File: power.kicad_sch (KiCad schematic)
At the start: 6 parts

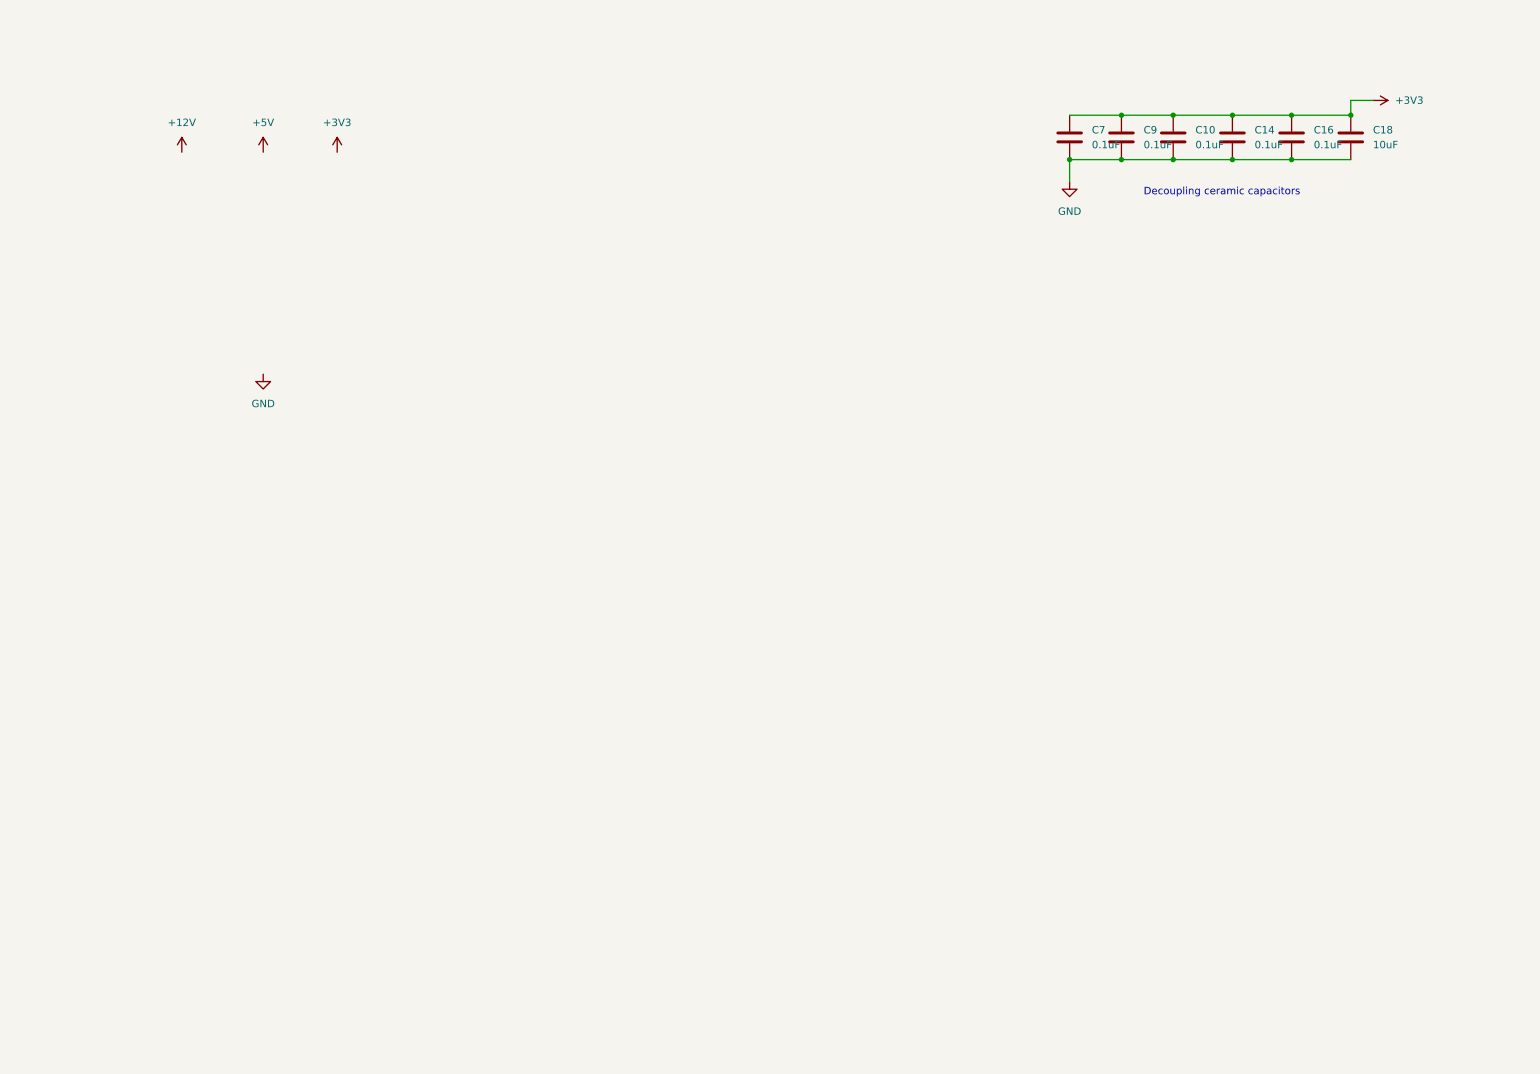
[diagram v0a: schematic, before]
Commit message: Add files via upload
changed 12v power to ICW6215, added 5 and 3v3
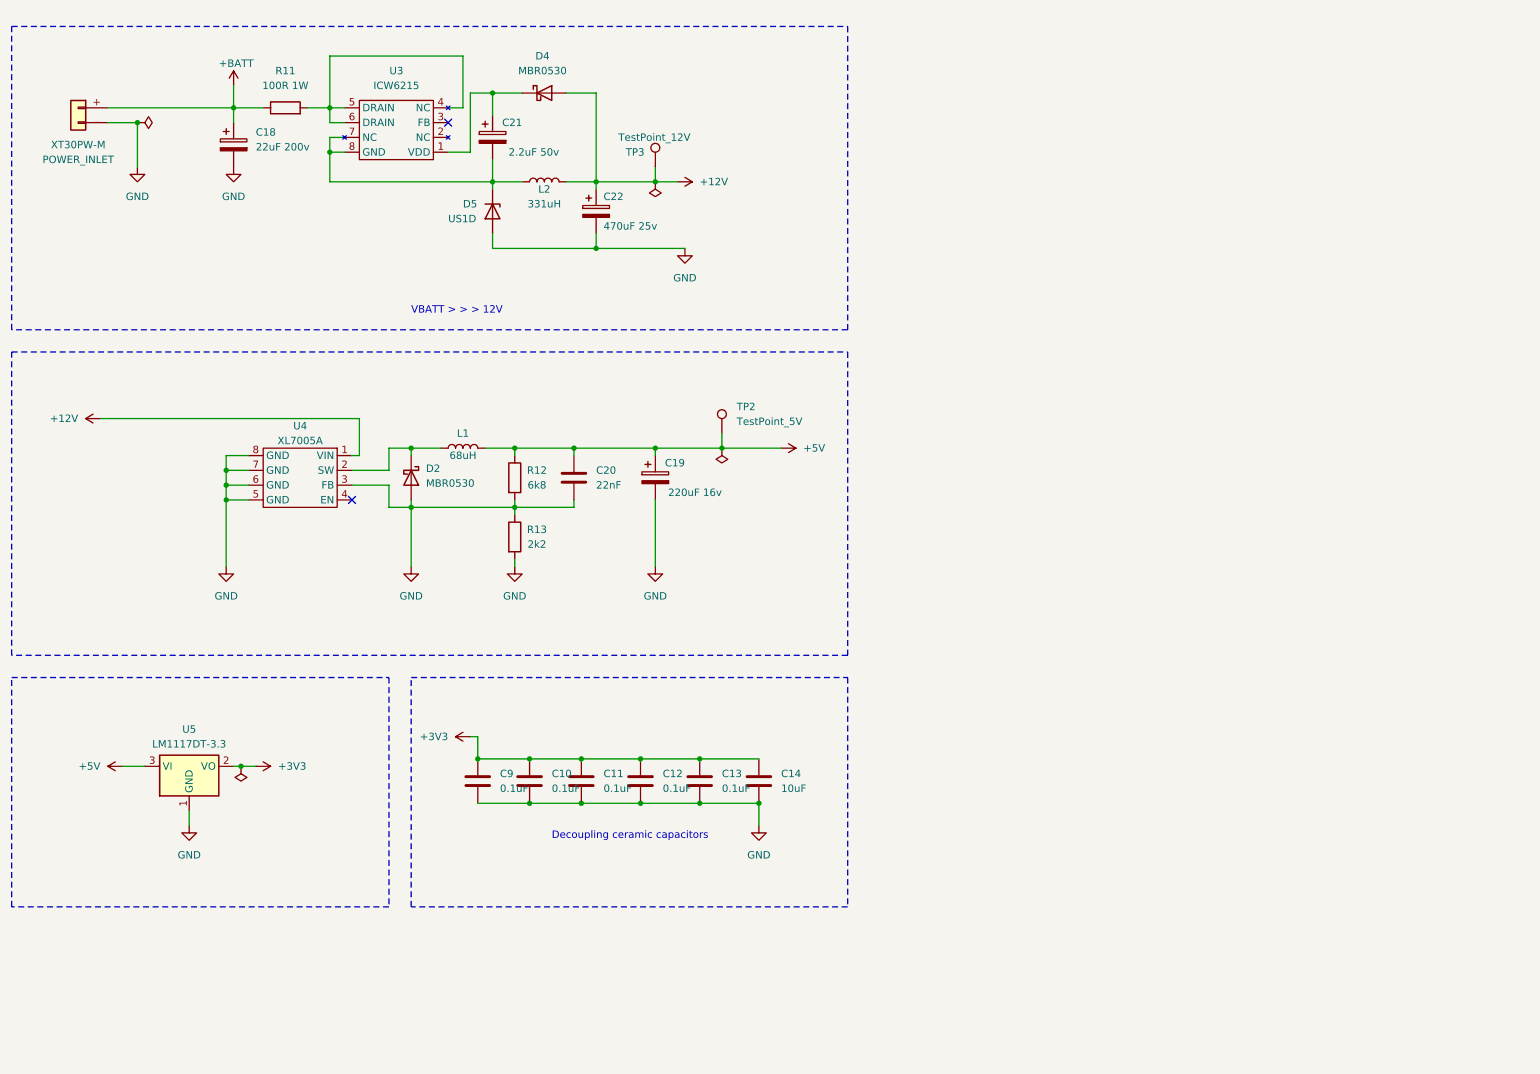
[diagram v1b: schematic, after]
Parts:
- added C18: 22uF 200v, symbol Device:C_Polarized
- added C19: 220uF 16v, symbol Device:C_Polarized
- added C20: 22nF, symbol Device:C
- added C21: 2.2uF 50v, symbol Device:C_Polarized
- added C22: 470uF 25v, symbol Device:C_Polarized
- added D2, D4: MBR0530, Diode_SMD:D_SOD-123, symbol Diode:MBR0530
- added D5: US1D, symbol Device:D_Zener
- added L1: 68uH, symbol Device:L
- added L2: 331uH, symbol Device:L
- added POWER_INLET: XT30PW-M, symbol Connector_Generic:Conn_01x02
- added R11: 100R 1W, symbol Device:R
- added R12: 6k8, symbol Device:R
- added R13: 2k2, symbol Device:R
- added TP2: TestPoint_5V, symbol Connector:TestPoint
- added TP3: TestPoint_12V, symbol Connector:TestPoint
- added U3: ICW6215, symbol 4shift:ICW6215
- added U4: XL7005A, symbol 4shift:XL7005a
- added U5: LM1117DT-3.3, Package_TO_SOT_SMD:TO-252-3_TabPin2, symbol Regulator_Linear:LM1117DT-3.3
- renumbered C9 to C10, C10 to C11, C14 to C12, C16 to C13, C18 to C14, C7 to C9
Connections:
- net +12V: now also C22.1, D4.2 (A), L2.2, TP3.1, U4.1 (VIN)
- net +3V3: now also U5.2 (VO)
- net +5V: now also C19.1, C20.1, L1.2, R12.1, TP2.1, U5.3 (VI)
- net GND: now also C18.2, C19.2, C20.2, C22.2, D2.2 (A), D5.2 (A), POWER_INLET._ (Pin_2), R12.2, R13.1, R13.2, U4.3 (FB), U4.5 (GND), U4.6 (GND), U4.7 (GND), U4.8 (GND), U5.1 (GND)
- new net: C21.1, D4.1 (K), U3.1 (VDD)
- new net: C21.2, D5.1 (K), L2.1, U3.7 (NC), U3.8 (GND)
- new net: R11.2, U3.4 (NC), U3.5 (DRAIN), U3.6 (DRAIN)
- new net: D2.1 (K), L1.1, U4.2 (SW)
- new net +BATT: C18.1, POWER_INLET.+ (Pin_1), R11.1
- no-connect marks 0 -> 2
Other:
- note added: "VBATT > > > 12V"
- moved on the sheet: C10, C11, C12, C13, C14, C9

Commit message: Add files via upload
Added hivoltage cirquit. TODO - add powon (VT19 on MSX)
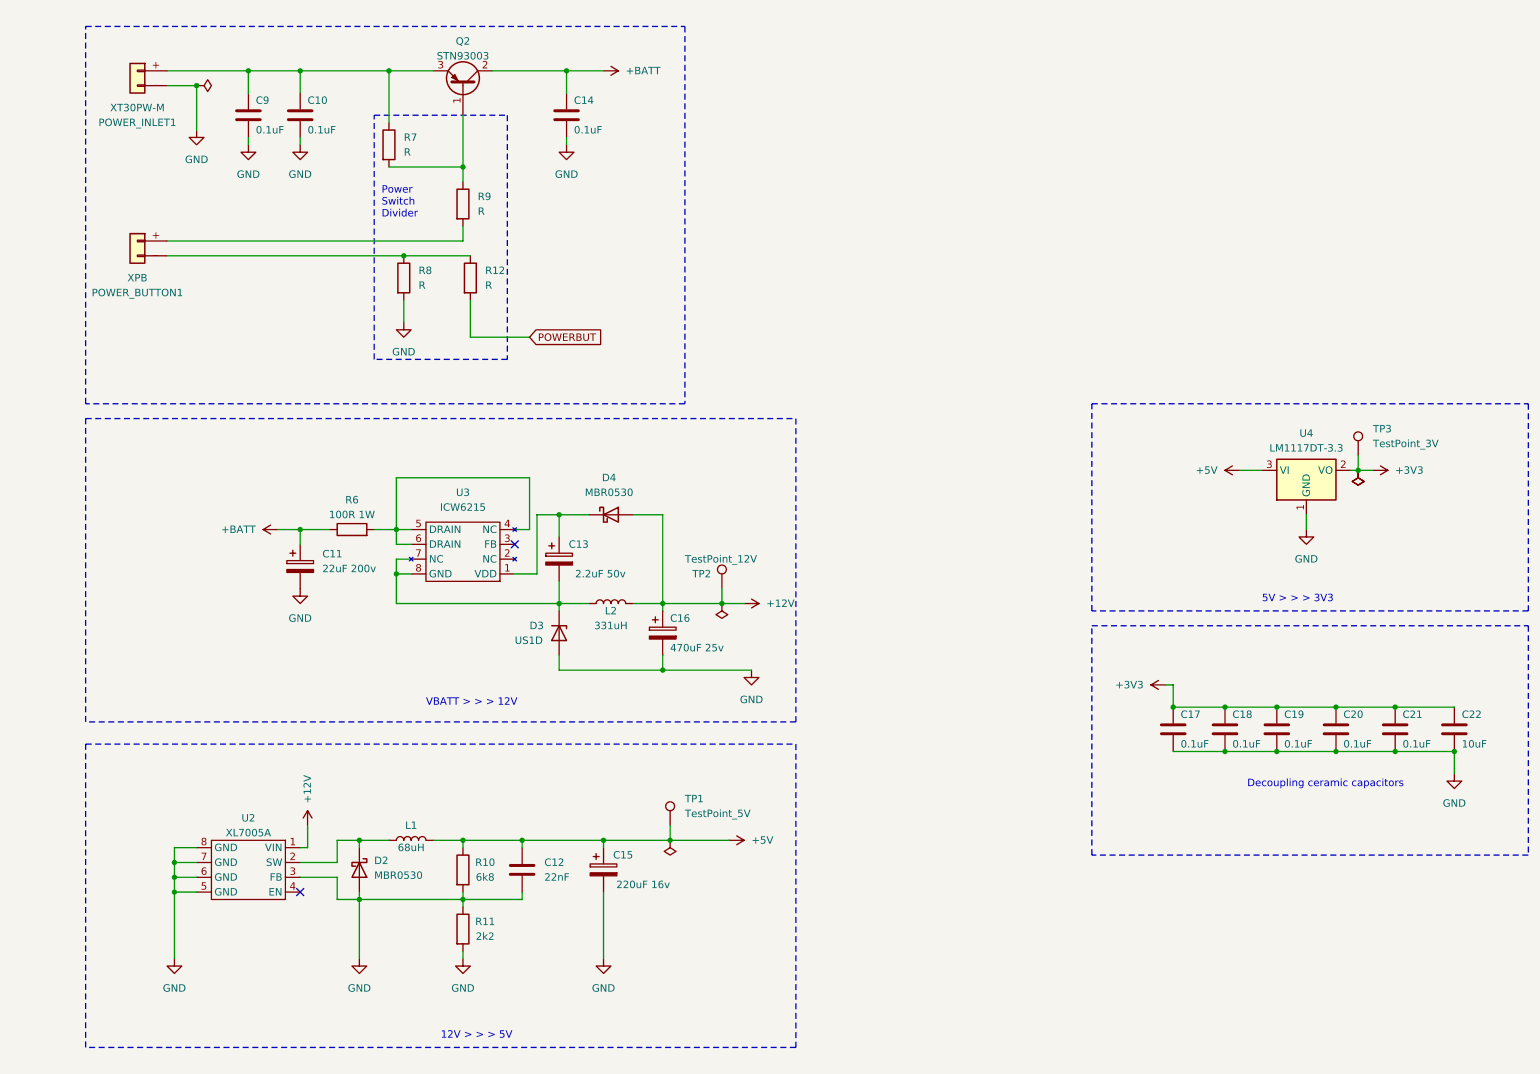
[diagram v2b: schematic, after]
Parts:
- removed POWER_INLET: XT30PW-M, symbol Connector_Generic:Conn_01x02
- removed U5: LM1117DT-3.3, Package_TO_SOT_SMD:TO-252-3_TabPin2, symbol Regulator_Linear:LM1117DT-3.3
- added C10, C14, C9: 0.1uF, Capacitor_SMD:C_0402_1005Metric, symbol Device:C
- added POWER_BUTTON1: XPB, symbol Connector_Generic:Conn_01x02
- added POWER_INLET1: XT30PW-M, symbol Connector_Generic:Conn_01x02
- added Q2: STN93003, Package_TO_SOT_SMD:SOT-223-3_TabPin2, symbol 4shift:STN93003
- added R12, R7, R8, R9: R, symbol Device:R
- added TP3: TestPoint_3V, symbol Connector:TestPoint
- added U4: LM1117DT-3.3, Package_TO_SOT_SMD:TO-252-3_TabPin2, symbol Regulator_Linear:LM1117DT-3.3
- renumbered C18 to C11, C20 to C12, C21 to C13, C19 to C15, C22 to C16, C9 to C17, C10 to C18, C11 to C19, C12 to C20, C13 to C21, C14 to C22, D5 to D3, R12 to R10, R13 to R11, R11 to R6, TP2 to TP1, TP3 to TP2, U4 to U2
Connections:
- net +3V3: now also TP3.1, U4.2 (VO)
- net +5V: now also U4.3 (VI)
- net +BATT: now also C14.1, Q2.2 (C)
- net GND: now also C10.2, C14.2, C9.2, POWER_INLET1._ (Pin_2), R8.2, U4.1 (GND)
- new net: C10.1, C9.1, POWER_INLET1.+ (Pin_1), Q2.3 (E), R7.1
- new net: Q2.1 (B), R7.2, R9.1
- new net: POWER_BUTTON1.+ (Pin_1), R9.2
- new net: POWER_BUTTON1._ (Pin_2), R12.1, R8.1
- new net POWERBUT: R12.2
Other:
- note added: "12V > > > 5V"
- note added: "5V > > > 3V3"
- note added: "Power Switch Divider"
- moved on the sheet: C11, C12, C13, C15, C16, C17, C18, C19, C20, C21, C22, D2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

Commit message: Add files via upload
Add +12 and +5 outlets, change buzzer transistor, minor updates
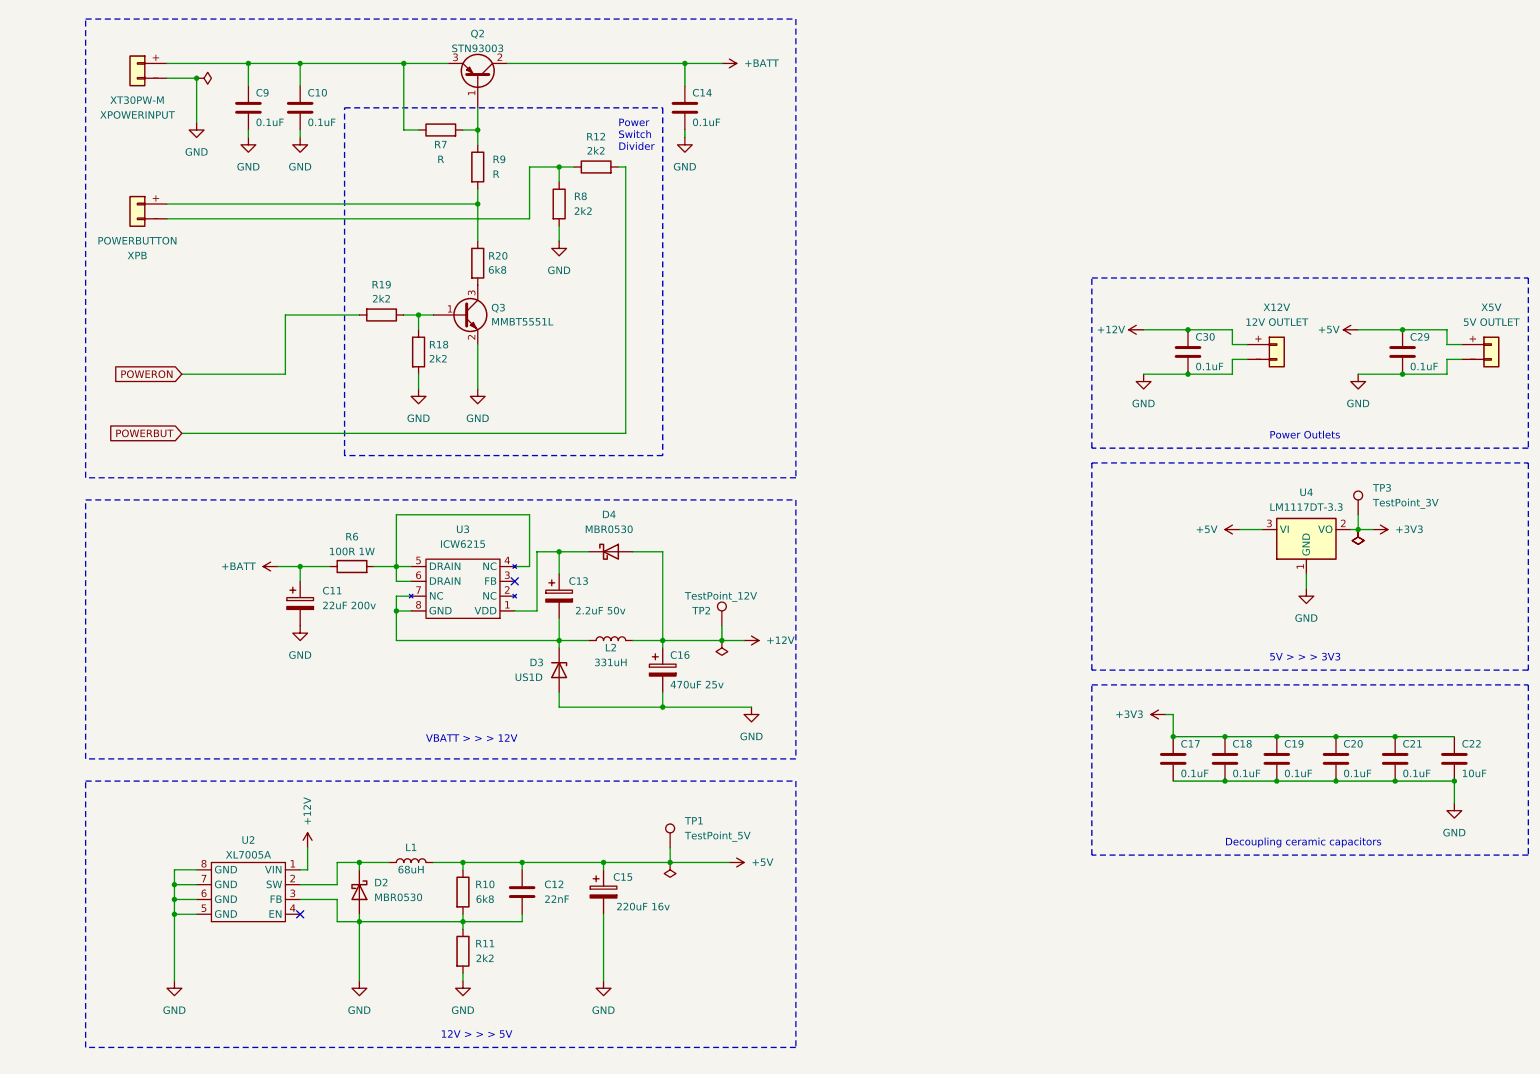
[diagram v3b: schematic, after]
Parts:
- added C29, C30: 0.1uF, Capacitor_SMD:C_0402_1005Metric, symbol Device:C
- added Q3: MMBT5551L, Package_TO_SOT_SMD:SOT-23, symbol Transistor_BJT:MMBT5551L
- added R18, R19: 2k2, symbol Device:R
- added R20: 6k8, symbol Device:R
- added X12V: 12V OUTLET, symbol Connector_Generic:Conn_01x02
- added X5V: 5V OUTLET, symbol Connector_Generic:Conn_01x02
- R12, R8: value R -> 2k2
- XPB: renamed from POWER_BUTTON1; value XPB -> POWERBUTTON
- renumbered POWER_INLET1 to XPOWERINPUT
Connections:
- net +12V: now also C30.1, X12V.+ (Pin_1)
- net +5V: now also C29.1, X5V.+ (Pin_1)
- net GND: now also C29.2, C30.2, Q3.2 (E), R18.2, X12V._ (Pin_2), X5V._ (Pin_2)
- net at R9.2, XPB.+ (Pin_1): now also R20.1
- new net: Q3.3 (C), R20.2
- new net: Q3.1 (B), R18.1, R19.1
- new net POWERON: R19.2
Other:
- note added: "Power Outlets"
- moved on the sheet: C10, C11, C12, C13, C14, C15, C16, C17, C18, C19, C20, C21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

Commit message: Divider, gate, mtr button, testpoints, minors
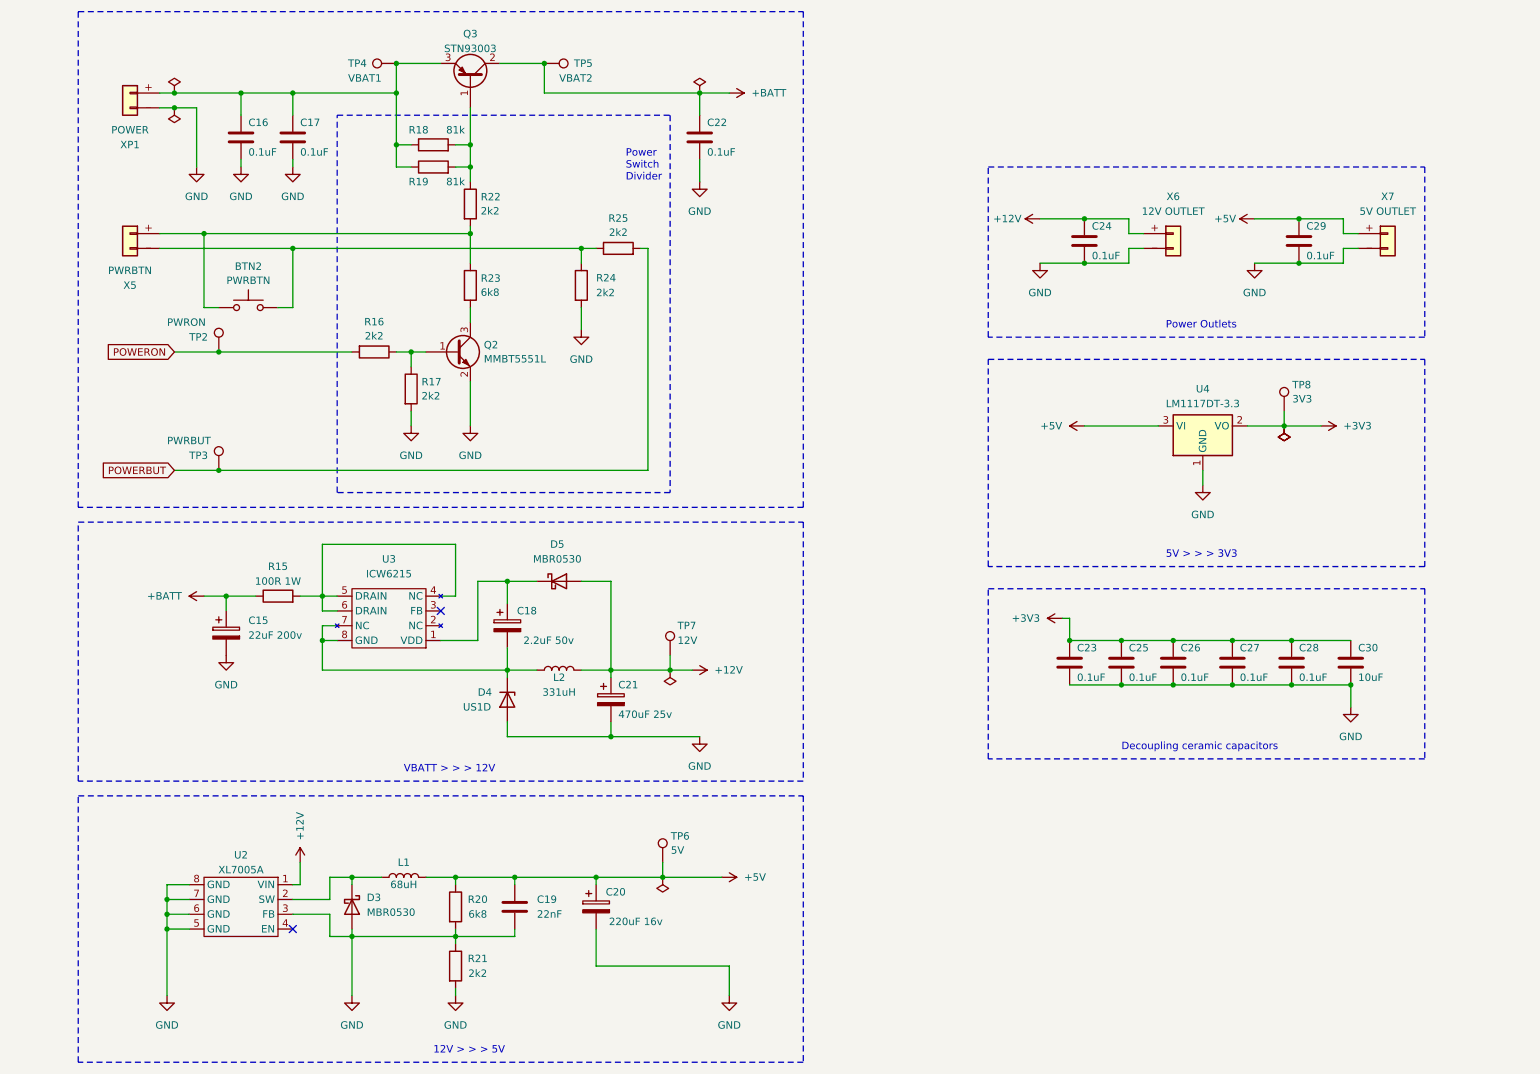
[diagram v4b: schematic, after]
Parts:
- added BTN2: PWRBTN, symbol Switch:SW_Push
- added R18: 81k, symbol Device:R
- added TP2: PWRON, symbol Connector:TestPoint
- added TP3: PWRBUT, symbol Connector:TestPoint
- added TP4: VBAT1, symbol Connector:TestPoint
- added TP5: VBAT2, symbol Connector:TestPoint
- R19: renamed from R7; value R -> 81k
- R22: renamed from R9; value R -> 2k2
- TP6: renamed from TP1; value TestPoint_5V -> 5V
- TP7: renamed from TP2; value TestPoint_12V -> 12V
- TP8: renamed from TP3; value TestPoint_3V -> 3V3
- X5: renamed from XPB; value POWERBUTTON -> PWRBTN
- XP1: renamed from XPOWERINPUT; value XT30PW-M -> POWER
- renumbered C11 to C15, C9 to C16, C10 to C17, C13 to C18, C12 to C19, C15 to C20, C16 to C21, C14 to C22, C17 to C23, C30 to C24, C18 to C25, C19 to C26, C20 to C27, C21 to C28, C22 to C30, D2 to D3, D3 to D4, D4 to D5, Q3 to Q2, Q2 to Q3, R6 to R15, R19 to R16, R18 to R17, R10 to R20, R11 to R21, R20 to R23, R8 to R24, R12 to R25, X12V to X6, X5V to X7
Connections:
- net +BATT: now also TP5.1
- net POWERBUT: now also TP3.1
- net POWERON: now also TP2.1
- net at R22.2, R23.1, X5.+ (Pin_1): now also BTN2.1
- net at C16.1, C17.1, Q3.3 (E)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: now also R18.1, TP4.1
- net at Q3.1 (B), R19.2, R22.1: now also R18.2
- net at R24.1, R25.1, X5._ (Pin_2): now also BTN2.2
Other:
- moved on the sheet: C15, C16, C17, C18, C19, C20, C21, C22, C23, C24, C25, C26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
